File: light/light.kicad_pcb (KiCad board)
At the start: 2 copper layers, 3 parts, among them J1 AVR_SPI, U1 ATMEGA8-16AU

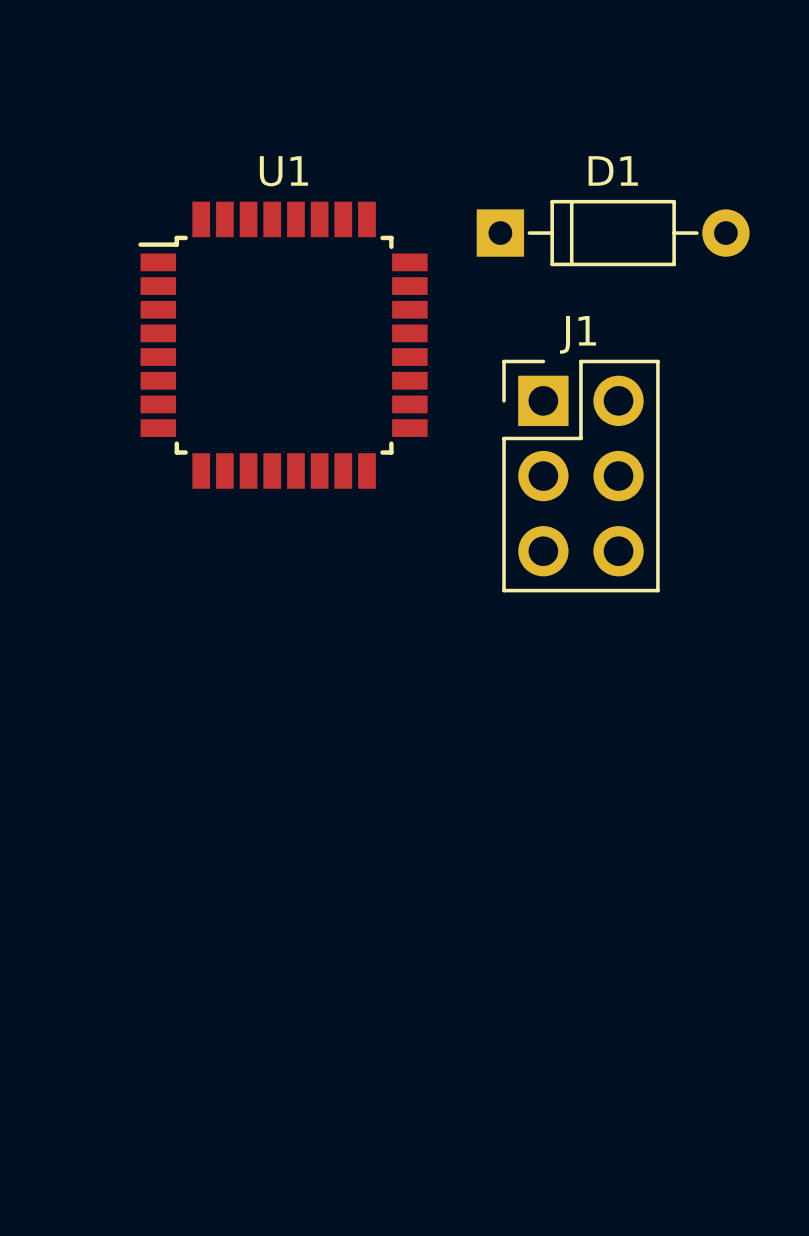
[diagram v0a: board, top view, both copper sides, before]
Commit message: Test uart tx
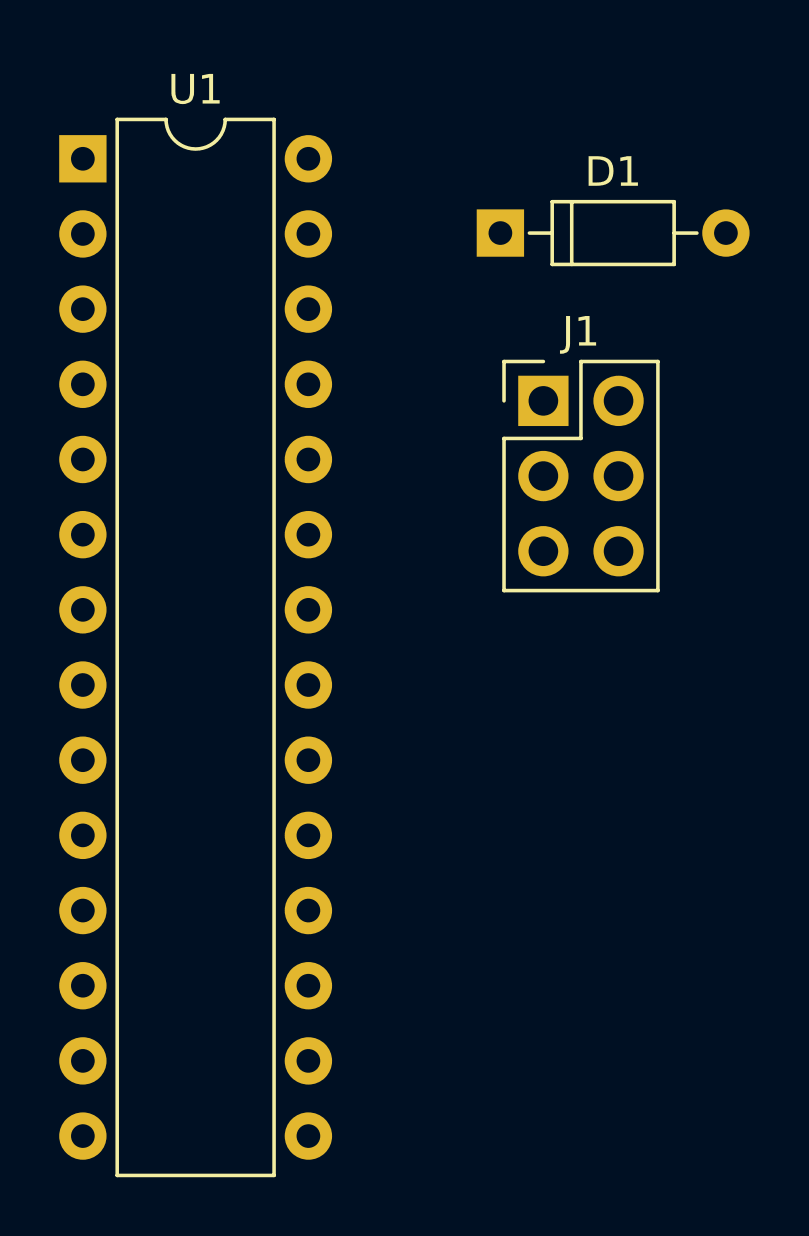
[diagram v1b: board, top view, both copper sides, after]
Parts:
- U1: value ATMEGA8-16AU -> ATMEGA8-16PU; footprint Housings_QFP:LQFP-32_7x7mm_Pitch0.8mm -> Housings_DIP:DIP-28_W7.62mm
- moved U1 9.27 mm to (112.3, 69.3)
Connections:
- U1 pad 1: Net-(U1-Pad1) -> /RES
- U1 pad 15: /MOSI -> Net-(U1-Pad15)
- U1 pad 16: /MISO -> Net-(U1-Pad16)
- U1 pad 17: /SCK -> /MOSI
- U1 pad 18: VCC -> /MISO
- U1 pad 19: Net-(U1-Pad19) -> /SCK
- U1 pad 20: Net-(U1-Pad20) -> VCC
- U1 pad 21: GND -> Net-(U1-Pad21)
- U1 pad 22: Net-(U1-Pad22) -> GND
- U1 pad 3: GND -> Net-(U1-Pad3)
- U1 pad 4: VCC -> /TX
- U1 pad 5: GND -> /RX
- U1 pad 6: VCC -> Net-(U1-Pad6)
- U1 pad 7: Net-(C2-Pad1) (its old number) -> VCC
- U1 pad 8: Net-(C3-Pad1) (its old number) -> GND
